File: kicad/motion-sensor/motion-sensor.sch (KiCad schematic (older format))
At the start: 32 parts, among them CON1 LUM 1613-14, CON2 LUM 1613-14, IC1 ATMEGA328P-A AU 1537, J1 RJ10_4p4c, J2 RJ10_4p4c, P1 ISP, P2 ESP8266, Q1 FDN337N, SW1 Motion-Sensor-1, SW2 Motion-Sensor-2, U1 MC34063, U2 Case

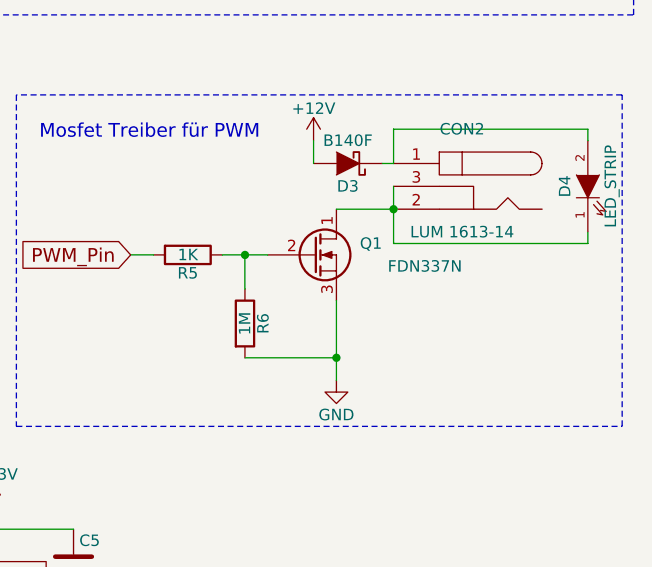
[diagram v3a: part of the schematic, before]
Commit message: motion sensor Projekt für Küche und unter dem Bett
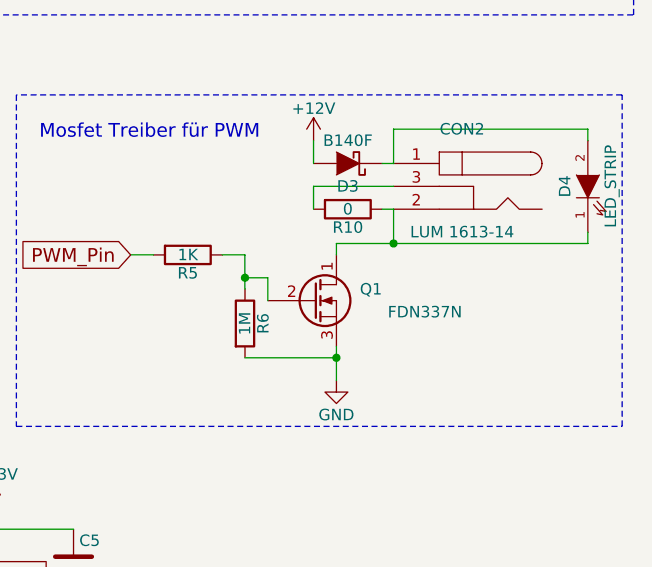
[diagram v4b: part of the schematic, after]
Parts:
- added R10: 0, Resistors_SMD:R_1206_HandSoldering, symbol R
- Q1: footprint TO_SOT_Packages_SMD:SOT-23_Handsoldering -> bolay library:SOT-23_Handsoldering-FDN-337N
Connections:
- net at CON2.2, D4.1 (K), Q1.1 (D): now also R10.1; no longer CON2.3
- new net: CON2.3, R10.2
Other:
- moved on the sheet: Q1
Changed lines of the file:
@@
 $EndComp
 $Comp
-L +12V #PWR01
+L +12V #PWR1
 U 1 1 56692781
 P 1200 1150
-F 0 "#PWR01" H 1200 1000 50  0001 C CNN
+F 0 "#PWR1" H 1200 1000 50  0001 C CNN
 F 1 "+12V" H 1200 1290 50  0000 C CNN
 F 2 "" H 1200 1150 50  0000 C CNN
@@
 $EndComp
 $Comp
-L GND #PWR02
+L GND #PWR2
 U 1 1 56693012
 P 1200 2350
-F 0 "#PWR02" H 1200 2100 50  0001 C CNN
+F 0 "#PWR2" H 1200 2100 50  0001 C CNN
 F 1 "GND" H 1200 2200 50  0000 C CNN
 F 2 "" H 1200 2350 50  0000 C CNN
@@
 $EndComp
 $Comp
-L +3.3V #PWR03
+L +3.3V #PWR12
 U 1 1 56693E9A
 P 4700 1250
-F 0 "#PWR03" H 4700 1100 50  0001 C CNN
+F 0 "#PWR12" H 4700 1100 50  0001 C CNN
 F 1 "+3.3V" H 4700 1390 50  0000 C CNN
 F 2 "" H 4700 1250 50  0000 C CNN
@@
 L Q_NMOS_DGS Q1
 U 1 1 56694EF9
-P 9400 4500
-F 0 "Q1" H 9700 4550 50  0000 R CNN
-F 1 "FDN337N" H 10050 4450 50  0000 R CNN
-F 2 "TO_SOT_Packages_SMD:SOT-23_Handsoldering" H 9600 4600 50  0001 C CNN
-F 3 "https://www.fairchildsemi.com/datasheets/FD/FDN337N.pdf" H 9400 4500 50  0001 C CNN
-F 4 "FDN337NTR-ND" H 9400 4500 60  0001 C CNN "Digi-Key"
-	1    9400 4500
-	1    0    0    -1
-$EndComp
-$Comp
-L GND #PWR04
+P 9400 4700
+F 0 "Q1" H 9700 4750 50  0000 R CNN
+F 1 "FDN337N" H 10050 4650 50  0000 R CNN
+F 2 "bolay library:SOT-23_Handsoldering-FDN-337N" H 9600 4800 50  0001 C CNN
+F 3 "https://www.fairchildsemi.com/datasheets/FD/FDN337N.pdf" H 9400 4700 50  0001 C CNN
+F 4 "FDN337NTR-ND" H 9400 4700 60  0001 C CNN "Digi-Key"
+	1    9400 4700
+	1    0    0    -1
+$EndComp
+$Comp
+L GND #PWR19
 U 1 1 56695647
 P 9500 5050
-F 0 "#PWR04" H 9500 4800 50  0001 C CNN
+F 0 "#PWR19" H 9500 4800 50  0001 C CNN
 F 1 "GND" H 9500 4900 50  0000 C CNN
 F 2 "" H 9500 5050 50  0000 C CNN
@@
 $EndComp
 $Comp
-L +3.3V #PWR05
+L +3.3V #PWR7
 U 1 1 56696591
 P 2900 3400
-F 0 "#PWR05" H 2900 3250 50  0001 C CNN
+F 0 "#PWR7" H 2900 3250 50  0001 C CNN
 F 1 "+3.3V" H 2900 3540 50  0000 C CNN
 F 2 "" H 2900 3400 50  0000 C CNN
@@
 $EndComp
 $Comp
-L GND #PWR06
+L GND #PWR8
 U 1 1 566965BA
 P 2900 6000
-F 0 "#PWR06" H 2900 5750 50  0001 C CNN
+F 0 "#PWR8" H 2900 5750 50  0001 C CNN
 F 1 "GND" H 2900 5850 50  0000 C CNN
 F 2 "" H 2900 6000 50  0000 C CNN
@@
 $EndComp
 $Comp
-L GND #PWR07
+L GND #PWR20
 U 1 1 566AFC0E
 P 9550 3100
-F 0 "#PWR07" H 9550 2850 50  0001 C CNN
+F 0 "#PWR20" H 9550 2850 50  0001 C CNN
 F 1 "GND" H 9550 2950 50  0000 C CNN
 F 2 "" H 9550 3100 50  0000 C CNN
@@
 $EndComp
 $Comp
-L +12V #PWR08
+L +12V #PWR18
 U 1 1 566B026D
 P 9400 4000
-F 0 "#PWR08" H 9400 3850 50  0001 C CNN
+F 0 "#PWR18" H 9400 3850 50  0001 C CNN
 F 1 "+12V" H 9400 4140 50  0000 C CNN
 F 2 "" H 9400 4000 50  0000 C CNN
@@
 RESET
 $Comp
-L +3.3V #PWR09
+L +3.3V #PWR10
 U 1 1 566B729E
 P 4400 7000
-F 0 "#PWR09" H 4400 6850 50  0001 C CNN
+F 0 "#PWR10" H 4400 6850 50  0001 C CNN
 F 1 "+3.3V" H 4400 7140 50  0000 C CNN
 F 2 "" H 4400 7000 50  0000 C CNN
@@
 $EndComp
 $Comp
-L GND #PWR010
+L GND #PWR11
 U 1 1 566B7663
 P 4400 7300
-F 0 "#PWR010" H 4400 7050 50  0001 C CNN
+F 0 "#PWR11" H 4400 7050 50  0001 C CNN
 F 1 "GND" H 4400 7150 50  0000 C CNN
 F 2 "" H 4400 7300 50  0000 C CNN
@@
 $EndComp
 $Comp
-L GND #PWR011
+L GND #PWR15
 U 1 1 566B2638
 P 7200 5900
-F 0 "#PWR011" H 7200 5650 50  0001 C CNN
+F 0 "#PWR15" H 7200 5650 50  0001 C CNN
 F 1 "GND" H 7200 5750 50  0000 C CNN
 F 2 "" H 7200 5900 50  0000 C CNN
@@
 $EndComp
 $Comp
-L GND #PWR012
+L GND #PWR14
 U 1 1 566B3930
 P 6100 2400
-F 0 "#PWR012" H 6100 2150 50  0001 C CNN
+F 0 "#PWR14" H 6100 2150 50  0001 C CNN
 F 1 "GND" H 6100 2250 50  0000 C CNN
 F 2 "" H 6100 2400 50  0000 C CNN
@@
 PWM_Pin
 $Comp
-L PWR_FLAG #FLG013
+L PWR_FLAG #FLG1
 U 1 1 566B6761
 P 1400 1200
-F 0 "#FLG013" H 1400 1295 50  0001 C CNN
+F 0 "#FLG1" H 1400 1295 50  0001 C CNN
 F 1 "PWR_FLAG" H 1400 1380 50  0000 C CNN
 F 2 "" H 1400 1200 50  0000 C CNN
@@
 $EndComp
 $Comp
-L PWR_FLAG #FLG014
+L PWR_FLAG #FLG2
 U 1 1 566B6917
 P 1450 2350
-F 0 "#FLG014" H 1450 2445 50  0001 C CNN
+F 0 "#FLG2" H 1450 2445 50  0001 C CNN
 F 1 "PWR_FLAG" H 1450 2530 50  0000 C CNN
 F 2 "" H 1450 2350 50  0000 C CNN
@@
 $EndComp
 $Comp
-L PWR_FLAG #FLG015
+L PWR_FLAG #FLG3
 U 1 1 566B6ECE
 P 4900 1250
-F 0 "#FLG015" H 4900 1345 50  0001 C CNN
+F 0 "#FLG3" H 4900 1345 50  0001 C CNN
 F 1 "PWR_FLAG" H 4900 1430 50  0000 C CNN
 F 2 "" H 4900 1250 50  0000 C CNN
@@
 NoConn ~ 3250 4200
 $Comp
-L +3.3V #PWR016
+L +3.3V #PWR16
 U 1 1 566C0F40
 P 8000 5600
-F 0 "#PWR016" H 8000 5450 50  0001 C CNN
+F 0 "#PWR16" H 8000 5450 50  0001 C CNN
 F 1 "+3.3V" H 8000 5740 50  0000 C CNN
 F 2 "" H 8000 5600 50  0000 C CNN
@@
 $EndComp
 $Comp
-L +3.3V #PWR017
+L +3.3V #PWR17
 U 1 1 566C1158
 P 8450 1350
-F 0 "#PWR017" H 8450 1200 50  0001 C CNN
+F 0 "#PWR17" H 8450 1200 50  0001 C CNN
 F 1 "+3.3V" H 8450 1490 50  0000 C CNN
 F 2 "" H 8450 1350 50  0000 C CNN
@@
 $EndComp
 $Comp
-L GND #PWR018
+L GND #PWR9
 U 1 1 566F4A0F
 P 3650 1750
-F 0 "#PWR018" H 3650 1500 50  0001 C CNN
+F 0 "#PWR9" H 3650 1500 50  0001 C CNN
 F 1 "GND" H 3650 1600 50  0000 C CNN
 F 2 "" H 3650 1750 50  0000 C CNN
@@
 $EndComp
 $Comp
-L GND #PWR019
+L GND #PWR13
 U 1 1 56693308
 P 4800 2350
-F 0 "#PWR019" H 4800 2100 50  0001 C CNN
+F 0 "#PWR13" H 4800 2100 50  0001 C CNN
 F 1 "GND" H 4800 2200 50  0000 C CNN
 F 2 "" H 4800 2350 50  0000 C CNN
@@
 	10600 4450 10600 4400
 Wire Wire Line
-	9750 4450 10600 4450
+	9500 4450 10600 4450
 Wire Wire Line
 	10600 3950 10600 4000
@@
 	9100 4950 9500 4950
 Wire Wire Line
-	9500 4700 9500 5050
-Connection ~ 9100 4500
+	9500 4900 9500 5050
 Wire Wire Line
 	9100 4650 9100 4500
 Wire Wire Line
-	9000 4500 9200 4500
+	9100 4500 9000 4500
 Wire Wire Line
 	1200 2350 1450 2350
@@
 $EndComp
 Wire Wire Line
-	9750 4200 9750 4450
-Wire Wire Line
-	9750 4300 9500 4300
-Wire Wire Line
 	9750 4100 9750 3950
-Connection ~ 9750 4300
 $Comp
 L D_Schottky D3
@@
 NoConn ~ 5150 4550
 $Comp
-L +3.3V #PWR020
+L +3.3V #PWR3
 U 1 1 56B23B4C
 P 1850 3400
-F 0 "#PWR020" H 1850 3250 50  0001 C CNN
+F 0 "#PWR3" H 1850 3250 50  0001 C CNN
 F 1 "+3.3V" H 1850 3540 50  0000 C CNN
 F 2 "" H 1850 3400 50  0000 C CNN
@@
 $EndComp
 $Comp
-L +3.3V #PWR021
+L +3.3V #PWR5
 U 1 1 56B23BAE
 P 2250 3400
-F 0 "#PWR021" H 2250 3250 50  0001 C CNN
+F 0 "#PWR5" H 2250 3250 50  0001 C CNN
 F 1 "+3.3V" H 2250 3540 50  0000 C CNN
 F 2 "" H 2250 3400 50  0000 C CNN
@@
 $EndComp
 $Comp
-L GND #PWR022
+L GND #PWR4
 U 1 1 56B23D32
 P 1850 4150
-F 0 "#PWR022" H 1850 3900 50  0001 C CNN
+F 0 "#PWR4" H 1850 3900 50  0001 C CNN
 F 1 "GND" H 1850 4000 50  0000 C CNN
 F 2 "" H 1850 4150 50  0000 C CNN
@@
 $EndComp
 $Comp
-L GND #PWR023
+L GND #PWR6
 U 1 1 56B23D94
 P 2250 4150
-F 0 "#PWR023" H 2250 3900 50  0001 C CNN
+F 0 "#PWR6" H 2250 3900 50  0001 C CNN
 F 1 "GND" H 2250 4000 50  0000 C CNN
 F 2 "" H 2250 4150 50  0000 C CNN
@@
 	1900 3900 1850 3900
 Connection ~ 1850 4050
+Wire Wire Line
+	9200 4600 9200 4700
+Wire Wire Line
+	9200 4600 9100 4600
+Connection ~ 9100 4600
+$Comp
+L R R10
+U 1 1 56C89AC4
+P 9550 4300
+F 0 "R10" V 9630 4300 50  0000 C CNN
+F 1 "0" V 9550 4300 50  0000 C CNN
+F 2 "Resistors_SMD:R_1206_HandSoldering" V 9480 4300 50  0001 C CNN
+F 3 "http://www.yageo.com.tw/exep/pages/download/literatures/PYu-R_INT-thick_7.pdf" H 9550 4300 50  0001 C CNN
+F 4 "311-0.0ERCT-ND" H 9550 4300 60  0001 C CNN "Digi-Key"
+	1    9550 4300
+	0    1    1    0
+$EndComp
+Wire Wire Line
+	9750 4300 9700 4300
+Wire Wire Line
+	9500 4450 9500 4500
+Connection ~ 9750 4450
+Wire Wire Line
+	9750 4200 9400 4200
+Wire Wire Line
+	9400 4200 9400 4300
+Wire Wire Line
+	9750 4450 9750 4300
 $EndSCHEMATC
